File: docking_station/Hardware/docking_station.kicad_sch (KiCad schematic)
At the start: 26 parts, among them IC1 VOM1271T, IC2 VOM1271T, J1 SUPPLY_EN, J2 LIVE_IN, J5 SUPPLY+, J6 SUPPLY-, K1 Fujitsu_FTR-LYCA005x, K2 EC2-3NU, K3 EC2-3NU, Q1 NMOS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

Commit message: docking_station draft finished
a lot to do still - mostly calculation and review, but the bulk is done and I'm happy
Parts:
- removed D8, D9: D, symbol Device:D
- removed RV1: Varistor, symbol Device:Varistor
- added D3, D4, D5, D6: D, symbol Device:D
- added F1: Fuse, symbol Device:Fuse
- added IC3, IC4, IC5: VOM1271T, SOP254P675X240-4N, symbol VOM1271T:VOM1271T
- added Q10, Q11: Q_NMOS_Depletion_DSG, symbol Device:Q_NMOS_Depletion_DSG
- added R3, R6, R7: R_Small, symbol Device:R_Small
- added R4: R_Shunt, symbol Device:R_Shunt
- added U2: Comparator, Package_TO_SOT_SMD:SOT-23-5, symbol Comparator:LM397
- added U3: ZXCT1086E5TA, Package_TO_SOT_SMD:SOT-23-5, symbol FIRO_collected:ZXCT1086E5TA
- K1: value Fujitsu_FTR-LYCA005x -> RELPOL R40N-3021-85-1024
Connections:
- net GND: now also Q9.1 (D), IC5.2 (K_1), R7.1, U2.2 (V-), U3.2 (GND); no longer Q8.1 (D)
- net LINE_A: now also Q8.1 (D), D4.1 (K), D6.2 (A), Q11.1 (D); no longer IC2.2 (K_1), Q9.1 (D)
- net LINE_B: now also K1.A1, D3.1 (K), D5.2 (A); no longer IC1.2 (K_1)
- net VDC: now also R4.1; no longer Q1.1 (D), U1.7 (Vdd), U1.8 (OUT)
- net at K3.12: now also D5.1 (K), D6.1 (K)
- net at IC1.4 (A_2), Q2.2 (G), Q3.2 (G): no longer Q4.2 (G), Q5.2 (G)
- net at IC1.3 (K_2), Q2.3 (S), Q3.3 (S): no longer Q4.3 (S), Q5.3 (S)
- net at K1.A2: now also Q10.1 (D)
- net at Q1.3 (S), U1.1 (IN): now also F1.2; no longer J5.1 (Pin_1)
- net at R1.1: now also IC3.1 (A_1); no longer IC2.1 (A_1)
- new net: IC3.2 (K_1), IC4.1 (A_1)
- new net: IC3.3 (K_2), Q6.3 (S), Q7.3 (S)
- new net: IC3.4 (A_2), Q6.2 (G), Q7.2 (G)
- new net: F1.1, J5.1 (Pin_1)
- new net: IC5.4 (A_2), Q10.2 (S), Q11.2 (S)
- new net: IC5.3 (K_2), Q10.3 (G), Q11.3 (G)
- new net: IC5.1 (A_1), R3.1
- new net: IC4.4 (A_2), Q8.2 (G), Q9.2 (G)
- new net: IC4.3 (K_2), Q8.3 (S), Q9.3 (S)
- new net: R6.2, R7.2, U2.1 (-)
- new net: IC1.2 (K_1), IC2.1 (A_1)
- new net: IC2.4 (A_2), Q4.2 (G), Q5.2 (G)
- new net: IC2.3 (K_2), Q4.3 (S), Q5.3 (S)
- new net: D3.2 (A), IC2.2 (K_1)
- new net: U2.3 (+), U3.1 (OUT)
- new net: R4.3, U3.3 (S+)
- new net: R4.2, U3.4 (S-)
- new net: D4.2 (A), IC4.2 (K_1)
- new net +24V: Q1.1 (D), R4.4, R6.1, U1.7 (Vdd), U1.8 (OUT), U2.5 (V+), U3.5 (VCC)
- new net NO_CURR: R3.2, U2.4
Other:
- note added: "ALTERNATIVE POLARITY MATCHING CIRCUIT"
- note added: "CURRENT MEASUREMENT CIRCUIT"
- note added: "POLARITY MATCHING CIRCUIT"
- note added: "SUPPLY CONTROL CIRCUIT"
- note added: "excl. from board"
- note added: "just a ref. voltage"
- note removed: "POLARITY SELECTION CIRCUIT"
- note removed: "SUPPLY STARTUP CIRCUIT"
- moved on the sheet: IC1, J1, J2, J5, J6, K1, Q1, Q2, Q3, Q4, Q5, R2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

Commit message: component_update
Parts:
- Q1, Q2, Q3, Q4, Q5, Q6, Q7, Q8, Q9: value NMOS -> SIDR392DP-T1-GE3; footprint (none) -> Package_SO:PowerPAK_SO-8_Single
- Q10, Q11: value Q_NMOS_Depletion_DSG -> DN2540N8-G
- R1, R2, R3: value R_Small -> 1k5
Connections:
- net GND: now also Q4.3 (D), Q9.3 (D); no longer Q4.1 (D), Q9.1 (D)
- net LINE_A: now also Q5.3 (D), Q8.3 (D); no longer Q2.1 (D), Q8.1 (D)
- net LINE_B: now also Q2.3 (D), Q7.3 (D); no longer Q5.1 (D), Q7.1 (D)
- net VDC: now also Q3.3 (D), Q6.3 (D); no longer Q3.1 (D), Q6.1 (D)
- net at IC1.4 (A_2), Q3.2 (G): now also Q5.2 (G); no longer Q2.2 (G)
- net at IC2.4 (A_2), Q4.2 (G): now also Q2.2 (G); no longer Q5.2 (G)
- new net: IC3.3 (K_2), Q6.1 (S), Q7.1 (S)
- new net: IC4.3 (K_2), Q8.1 (S), Q9.1 (S)
- new net: IC2.3 (K_2), Q2.1 (S), Q4.1 (S)
- new net: IC1.3 (K_2), Q3.1 (S), Q5.1 (S)
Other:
- moved on the sheet: D3, D4, IC1, IC2, IC3, IC4, Q10, Q3, R2, R4, R6, R7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

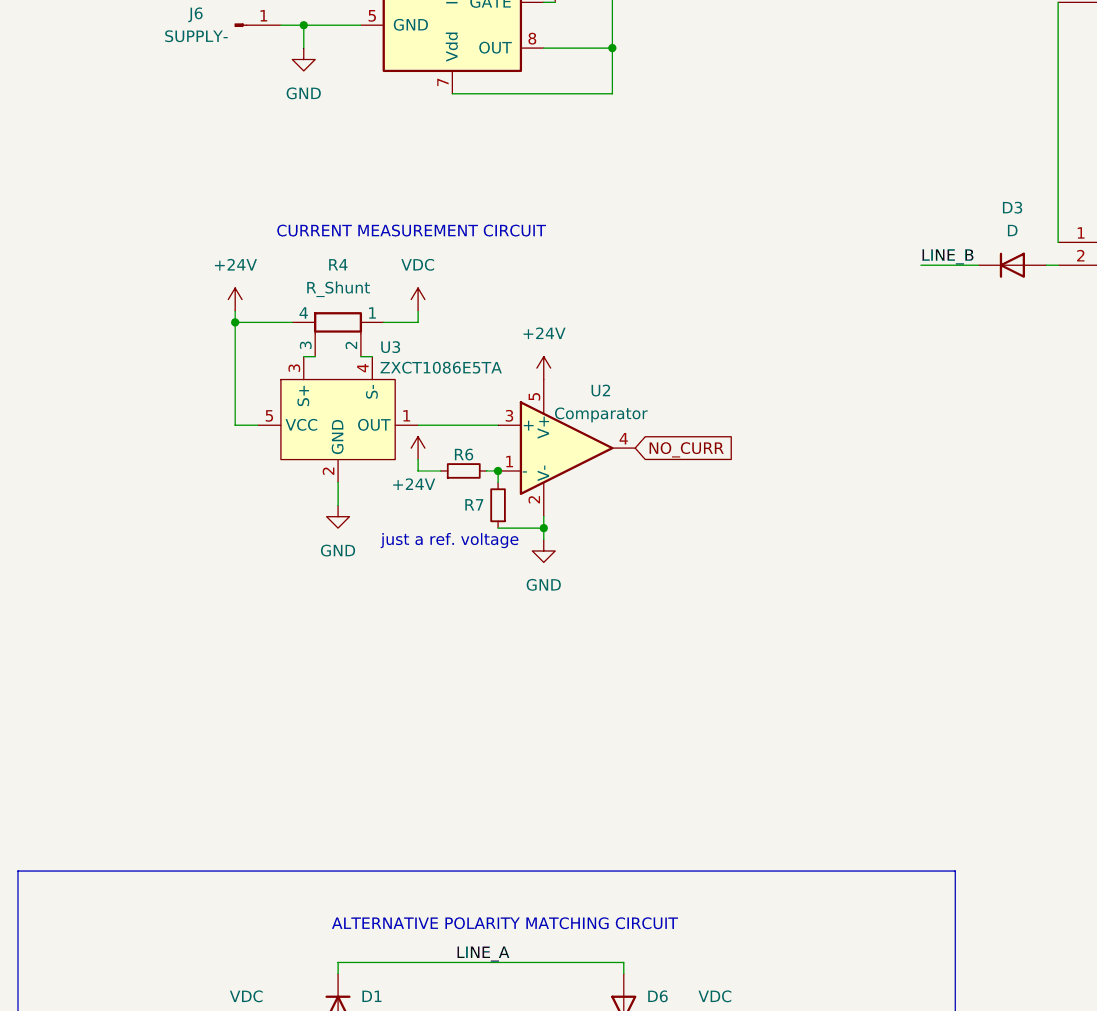
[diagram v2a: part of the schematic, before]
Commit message: more components chosen
it's a case of finishing the component choices and exporting the BOM now
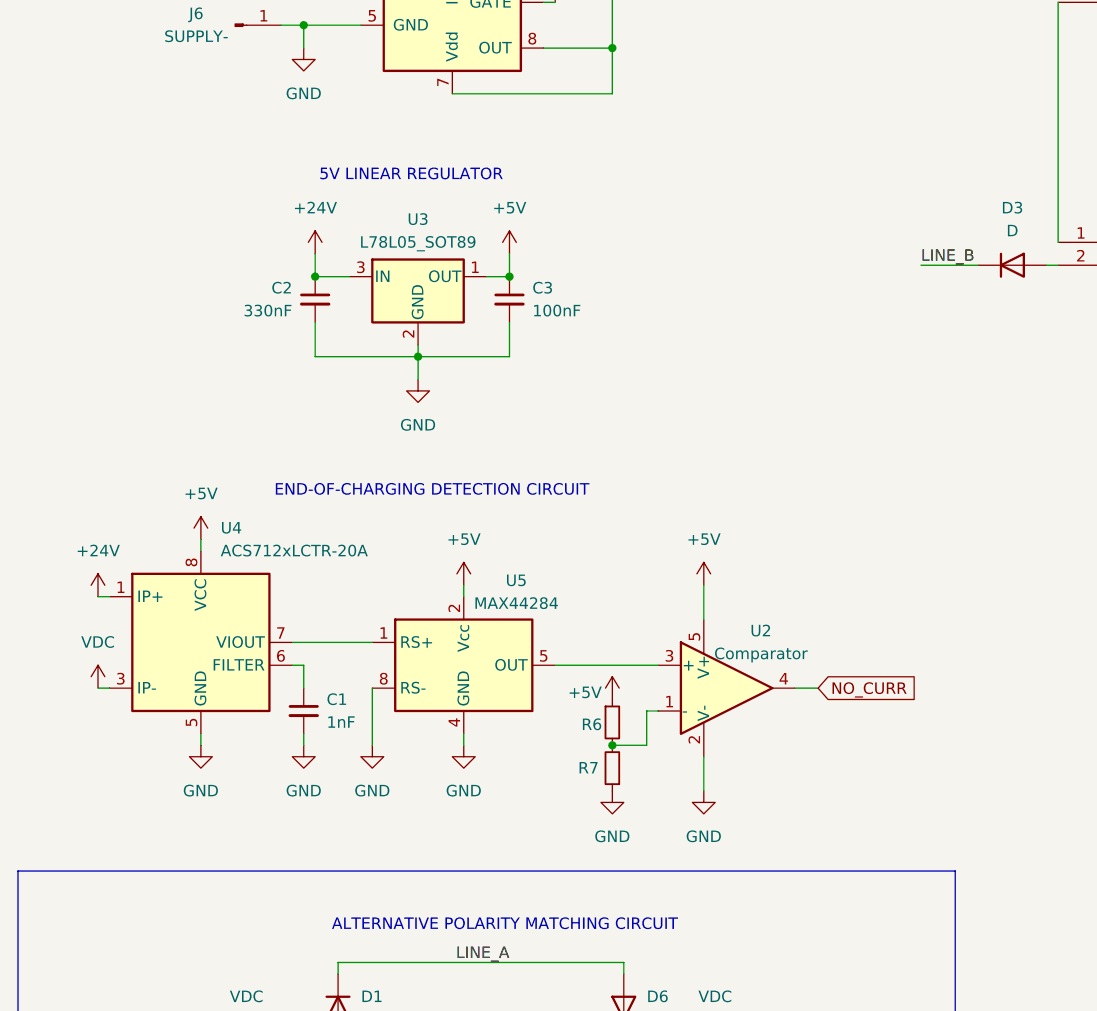
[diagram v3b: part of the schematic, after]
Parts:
- removed R4: R_Shunt, symbol Device:R_Shunt
- removed U3: ZXCT1086E5TA, Package_TO_SOT_SMD:SOT-23-5, symbol FIRO_collected:ZXCT1086E5TA
- added C1: 1nF, symbol Device:C_Small
- added C2: 330nF, symbol Device:C_Small
- added C3: 100nF, symbol Device:C_Small
- added U3: L78L05_SOT89, Package_TO_SOT_SMD:SOT-89-3, symbol Regulator_Linear:L78L05_SOT89
- added U4: ACS712xLCTR-20A, Package_SO:SOIC-8_3.9x4.9mm_P1.27mm, symbol Sensor_Current:ACS712xLCTR-20A
- added U5: MAX44284, symbol FIRO_collected:MAX44284
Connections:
- net +24V: now also C2.1, U3.3 (IN), U4.1 (IP+), U4.2 (IP+); no longer R6.1, U2.5 (V+)
- net GND: now also C1.2, C2.2, C3.2, U3.2 (GND), U4.5 (GND), U5.4 (GND), U5.8 (RS-)
- net VDC: now also U4.3 (IP-), U4.4 (IP-)
- net at U2.3 (+): now also U5.5 (OUT)
- new net: C1.1, U4.6 (FILTER)
- new net: U4.7 (VIOUT), U5.1 (RS+)
- new net +5V: C3.1, R6.1, U2.5 (V+), U3.1 (OUT), U4.8 (VCC), U5.2 (Vcc)
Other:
- note added: "5V LINEAR REGULATOR"
- note added: "END-OF-CHARGING DETECTION CIRCUIT"
- note removed: "CURRENT MEASUREMENT CIRCUIT"
- note removed: "just a ref. voltage"
- moved on the sheet: R6, R7, U2

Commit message: minor update
some changes to the cutoff circuit
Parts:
- removed R6, R7: R_Small, symbol Device:R_Small
- removed U5: MAX44284, symbol FIRO_collected:MAX44284
- added R4: 1k, symbol Device:R_Small
- added R5: 100k, symbol Device:R_Small
- added RV1: R_Potentiometer, symbol Device:R_Potentiometer
- added U5: ${SIM.PARAMS}, symbol Simulation_SPICE:OPAMP
- U3: value L78L05_SOT89 -> L78L05AB
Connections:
- net +5V: now also RV1.1, U5.3 (V+)
- net GND: now also R4.2, RV1.3, U5.4 (V-)
- net at U2.1 (-): now also RV1.2
- net at U2.3 (+): now also R5.2, U5.5
- net at U4.7 (VIOUT): now also U5.1 (+)
- new net: R4.1, R5.1, U5.2 (-)
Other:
- note added: "100n albo 10n!"
- note added: "DECOUPLING!!!!!"
- note added: "FLYBACK!!!"
- note added: "WYBRAĆ OPAMPA I KOMPARATOR"
- moved on the sheet: C1, C2, C3, U2, U3, U4

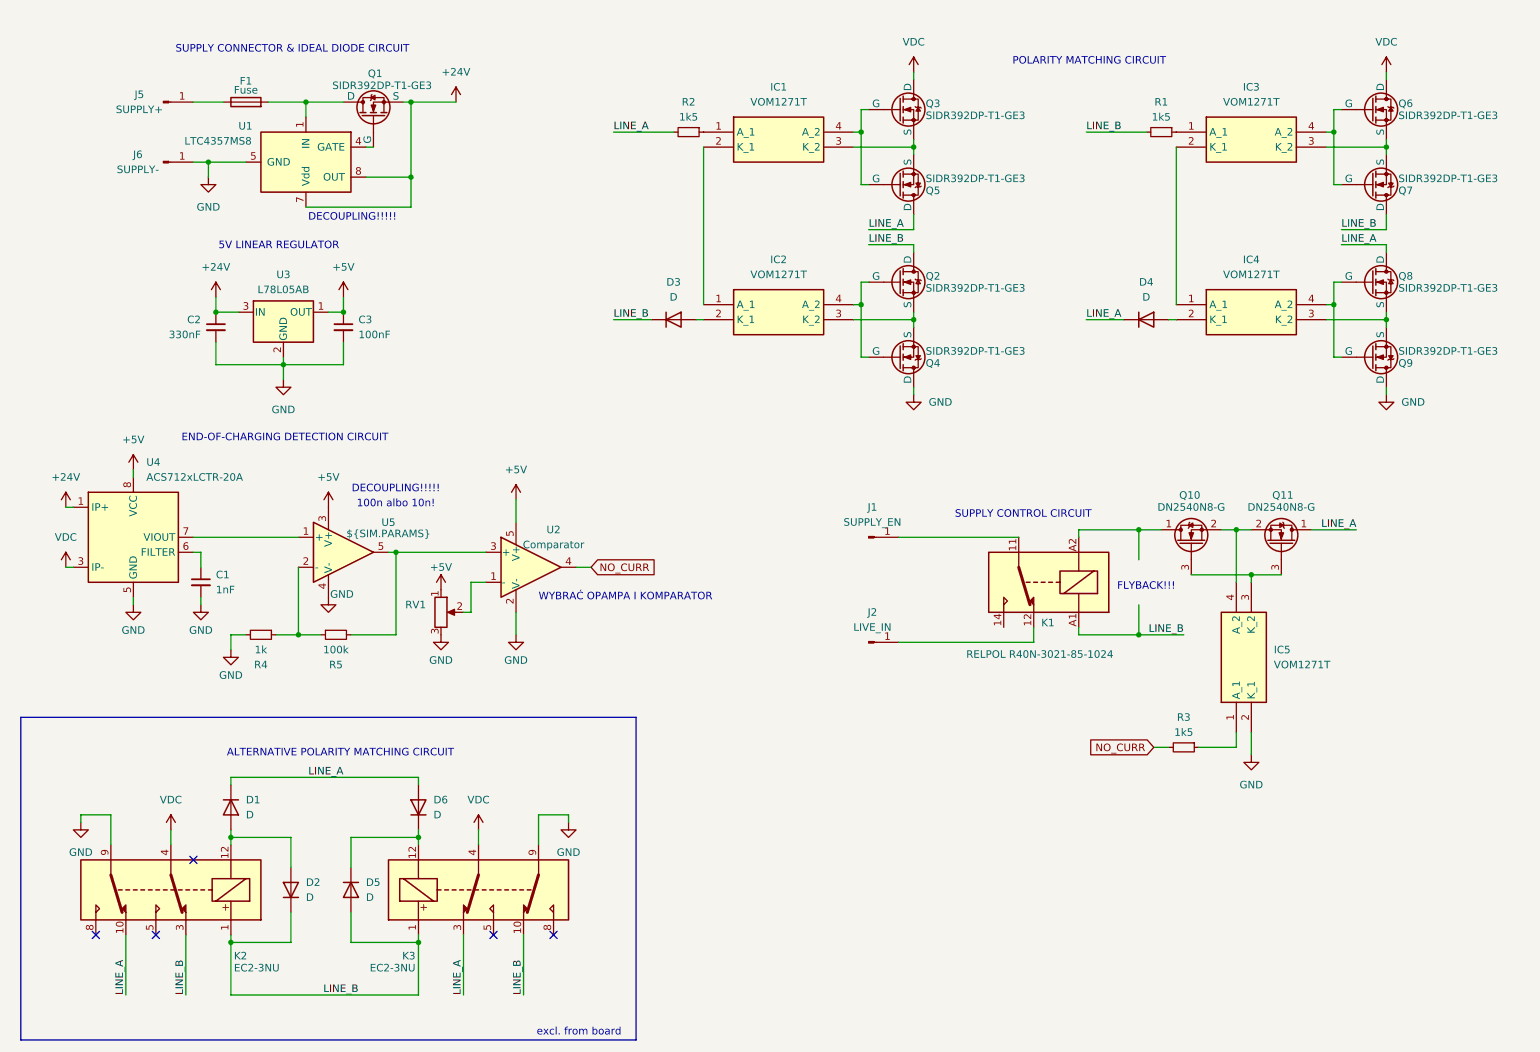
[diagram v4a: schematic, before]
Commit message: minor update to current sensing circuit
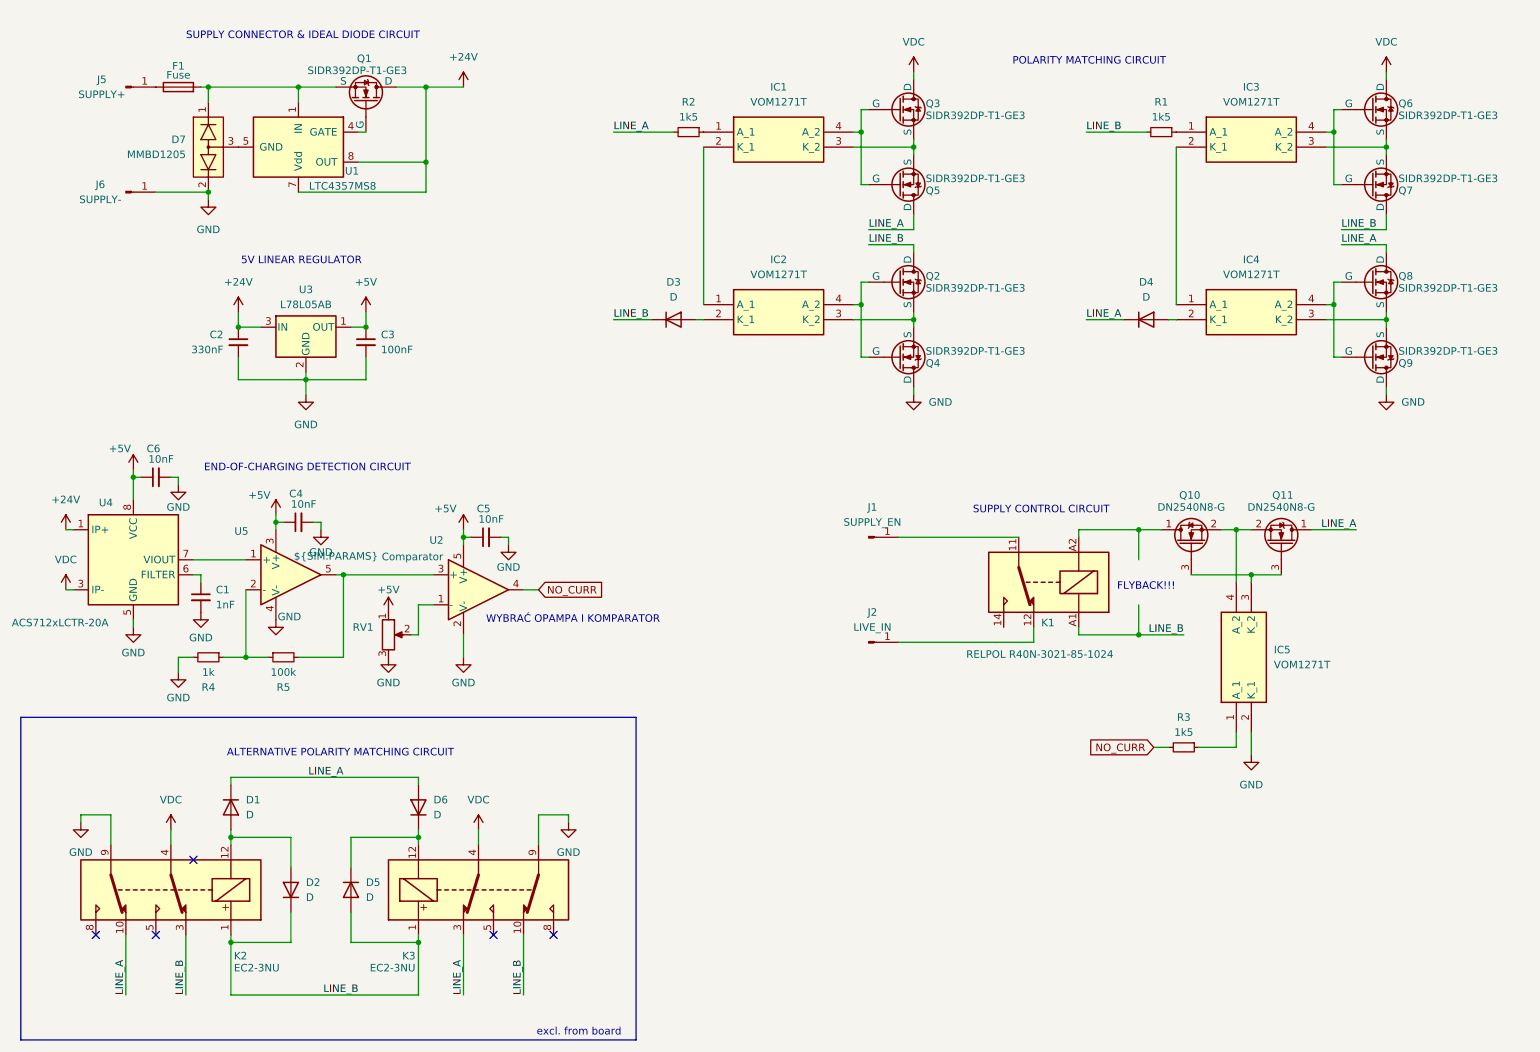
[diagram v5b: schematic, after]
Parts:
- added C4, C5, C6: 10nF, symbol Device:C_Small
- added D7: MMBD1205, Package_TO_SOT_SMD:SOT-23, symbol FIRO_collected:MMBD1205
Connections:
- net +24V: now also Q1.3 (D); no longer Q1.1 (S)
- net +5V: now also C4.1, C5.1, C6.1
- net GND: now also C4.2, C5.2, C6.2, D7.2; no longer U1.5 (GND)
- net at F1.2, U1.1 (IN): now also Q1.1 (S), D7.1; no longer Q1.3 (D)
- new net: D7.3, U1.5 (GND)
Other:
- note removed: "100n albo 10n!"
- note removed: "DECOUPLING!!!!!"
- moved on the sheet: C1, C2, C3, J5, J6, Q1, R4, R5, RV1, U1, U2, U3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

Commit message: major end-of-charging detector update
That was overwhelming, but will work. I hope. Lots of simulations before me
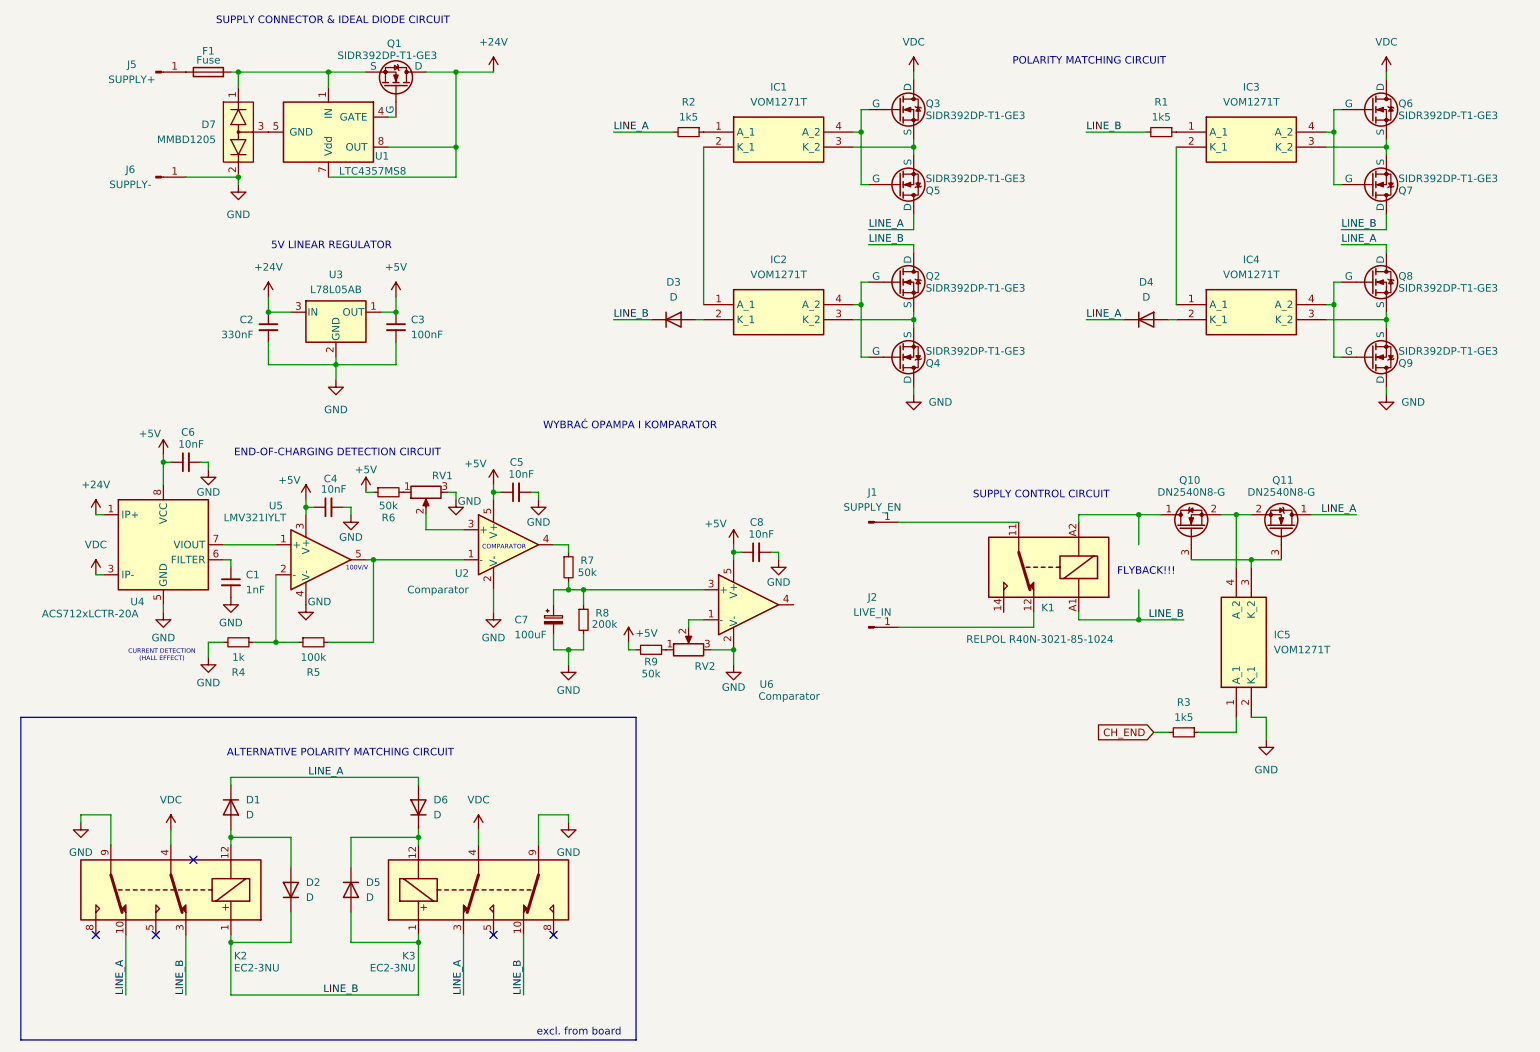
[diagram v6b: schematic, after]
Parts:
- added C7: 100uF, symbol Device:C_Polarized_Small
- added C8: 10nF, symbol Device:C_Small
- added R6, R7, R9: 50k, symbol Device:R_Small
- added R8: 200k, symbol Device:R_Small
- added RV2: R_Potentiometer, symbol Device:R_Potentiometer
- added U6: Comparator, Package_TO_SOT_SMD:SOT-23-5, symbol Comparator:LM397
- U5: value ${SIM.PARAMS} -> LMV321IYLT; footprint (none) -> Package_TO_SOT_SMD:SOT-23
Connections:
- net +5V: now also C8.1, R6.1, R9.2, U6.5 (V+); no longer RV1.1
- net GND: now also C7.2, C8.2, R8.2, RV2.3, U6.2 (V-)
- net at U2.1 (-): now also R5.2, U5.5; no longer RV1.2
- net NO_CURR: no longer names the net of U2.4
- net NO_CURR: now also R7.1; no longer R3.2
- new net: C7.1, R7.2, R8.1, U6.3 (+)
- new net: R9.1, RV2.1
- new net: RV2.2, U6.1 (-)
- new net: RV1.2, U2.3 (+)
- new net: R6.2, RV1.1
- new net CH_END: R3.2
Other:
- note added: "100V/V"
- note added: "COMPARATOR"
- note added: "CURRENT DETECTION (HALL EFFECT)"
- moved on the sheet: C1, C2, C3, C4, C5, C6, D7, F1, IC5, J1, J2, J5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
